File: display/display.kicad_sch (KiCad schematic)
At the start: 19 parts, among them J1 DIN41612_03x32_ABC

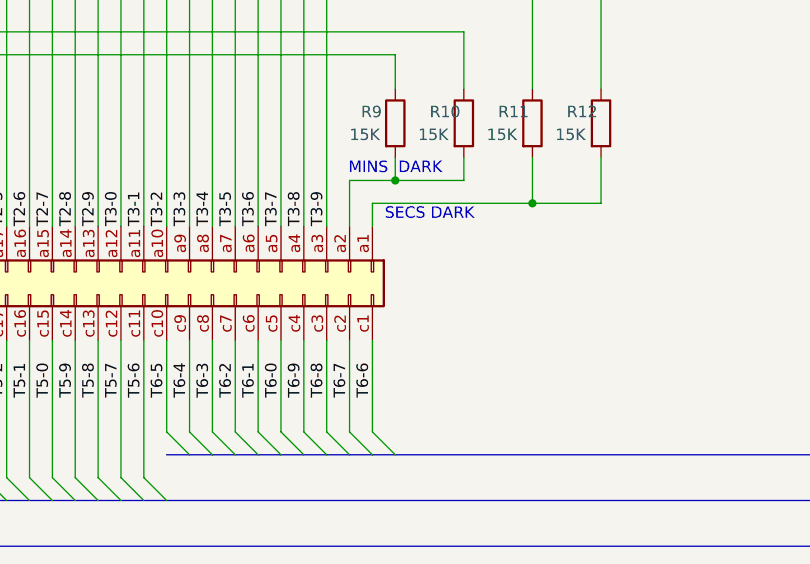
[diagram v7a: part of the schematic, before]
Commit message: Proposed final display board positioning
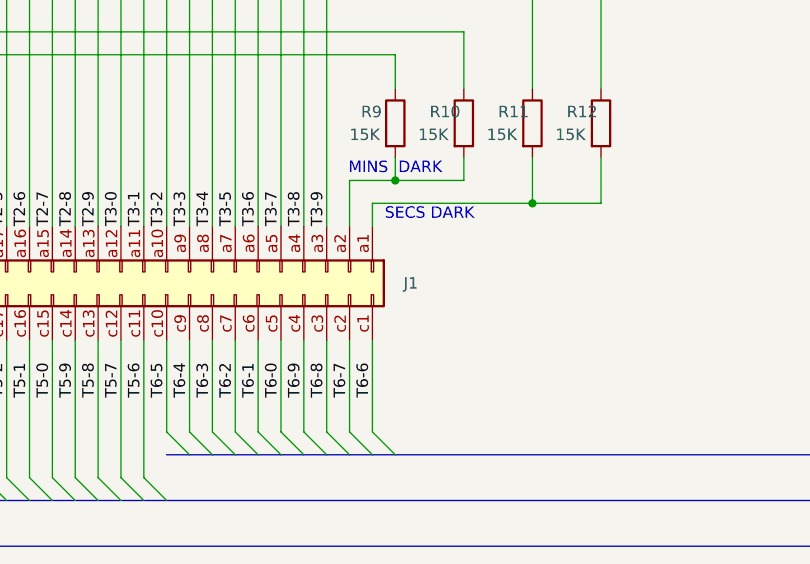
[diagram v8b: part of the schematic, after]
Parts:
- R1, R10, R11, R12, R2, R3, R4, R5, R6, R7, R8, R9: footprint Resistor_THT:R_Box_L14.0mm_W5.0mm_P9.00mm -> Resistor_THT:R_Box_L13.0mm_W4.0mm_P9.00mm
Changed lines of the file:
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@@
 			)
 		)
-		(property "Footprint" "Resistor_THT:R_Box_L14.0mm_W5.0mm_P9.00mm"
+		(property "Footprint" "Resistor_THT:R_Box_L13.0mm_W4.0mm_P9.00mm"
 			(at 75.692 93.98 90)
 			(effects
@@
 			)
 		)
-		(property "Footprint" "Resistor_THT:R_Box_L14.0mm_W5.0mm_P9.00mm"
+		(property "Footprint" "Resistor_THT:R_Box_L13.0mm_W4.0mm_P9.00mm"
 			(at 224.282 93.98 90)
 			(effects
@@
 			)
 		)
-		(property "Footprint" "Resistor_THT:R_Box_L14.0mm_W5.0mm_P9.00mm"
+		(property "Footprint" "Resistor_THT:R_Box_L13.0mm_W4.0mm_P9.00mm"
 			(at 165.862 54.61 90)
 			(effects
@@
 			)
 		)
-		(property "Footprint" "Resistor_THT:R_Box_L14.0mm_W5.0mm_P9.00mm"
+		(property "Footprint" "Resistor_THT:R_Box_L13.0mm_W4.0mm_P9.00mm"
 			(at 66.802 93.98 90)
 			(effects
@@
 			)
 		)
-		(property "Footprint" "Resistor_THT:R_Box_L14.0mm_W5.0mm_P9.00mm"
+		(property "Footprint" "Resistor_THT:R_Box_L13.0mm_W4.0mm_P9.00mm"
 			(at 209.042 93.98 90)
 			(effects
@@
 		(on_board yes)
 		(dnp no)
-		(fields_autoplaced yes)
 		(property "Reference" "J1"
-			(at 86.36 110.4899 90)
+			(at 213.36 111.76 90)
 			(effects
 				(font
@@
 				)
 				(justify right)
-				(hide yes)
 			)
 		)
@@
 			)
 		)
-		(property "Footprint" "Resistor_THT:R_Box_L14.0mm_W5.0mm_P9.00mm"
+		(property "Footprint" "Resistor_THT:R_Box_L13.0mm_W4.0mm_P9.00mm"
 			(at 216.662 93.98 90)
 			(effects
@@
 			)
 		)
-		(property "Footprint" "Resistor_THT:R_Box_L14.0mm_W5.0mm_P9.00mm"
+		(property "Footprint" "Resistor_THT:R_Box_L13.0mm_W4.0mm_P9.00mm"
 			(at 123.952 54.61 90)
 			(effects
@@
 			)
 		)
-		(property "Footprint" "Resistor_THT:R_Box_L14.0mm_W5.0mm_P9.00mm"
+		(property "Footprint" "Resistor_THT:R_Box_L13.0mm_W4.0mm_P9.00mm"
 			(at 35.052 54.61 90)
 			(effects
@@
 			)
 		)
-		(property "Footprint" "Resistor_THT:R_Box_L14.0mm_W5.0mm_P9.00mm"
+		(property "Footprint" "Resistor_THT:R_Box_L13.0mm_W4.0mm_P9.00mm"
 			(at 207.772 54.61 90)
 			(effects
@@
 			)
 		)
-		(property "Footprint" "Resistor_THT:R_Box_L14.0mm_W5.0mm_P9.00mm"
+		(property "Footprint" "Resistor_THT:R_Box_L13.0mm_W4.0mm_P9.00mm"
 			(at 231.902 93.98 90)
 			(effects
@@
 			)
 		)
-		(property "Footprint" "Resistor_THT:R_Box_L14.0mm_W5.0mm_P9.00mm"
+		(property "Footprint" "Resistor_THT:R_Box_L13.0mm_W4.0mm_P9.00mm"
 			(at 80.772 54.61 90)
 			(effects
@@
 			)
 		)
-		(property "Footprint" "Resistor_THT:R_Box_L14.0mm_W5.0mm_P9.00mm"
+		(property "Footprint" "Resistor_THT:R_Box_L13.0mm_W4.0mm_P9.00mm"
 			(at 249.682 54.61 90)
 			(effects
